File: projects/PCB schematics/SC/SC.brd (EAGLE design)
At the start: 160 x 100 mm, 19 parts

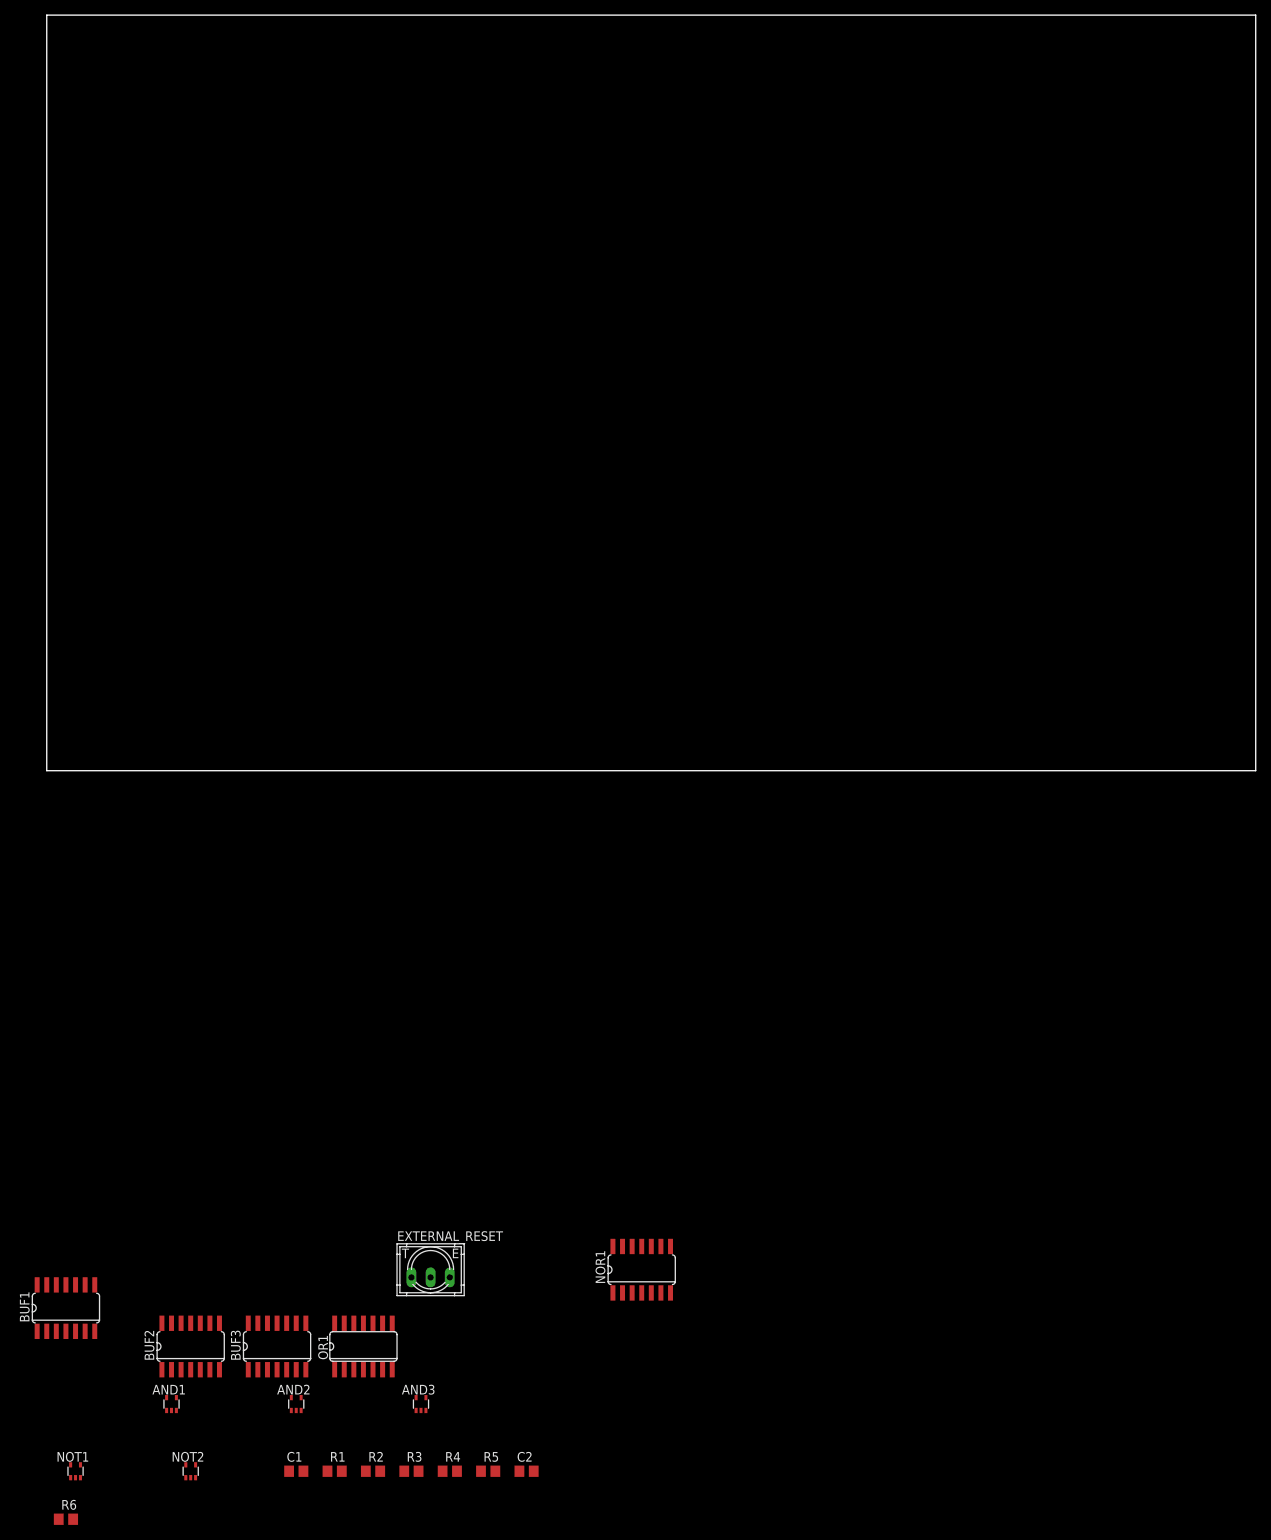
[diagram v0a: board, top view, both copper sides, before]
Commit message: SC - Rev A; First PCB revision complete.
This marks the first draft of the SC board.
Parts have been laid out and initial routing completed through
extensive use of autorouter.
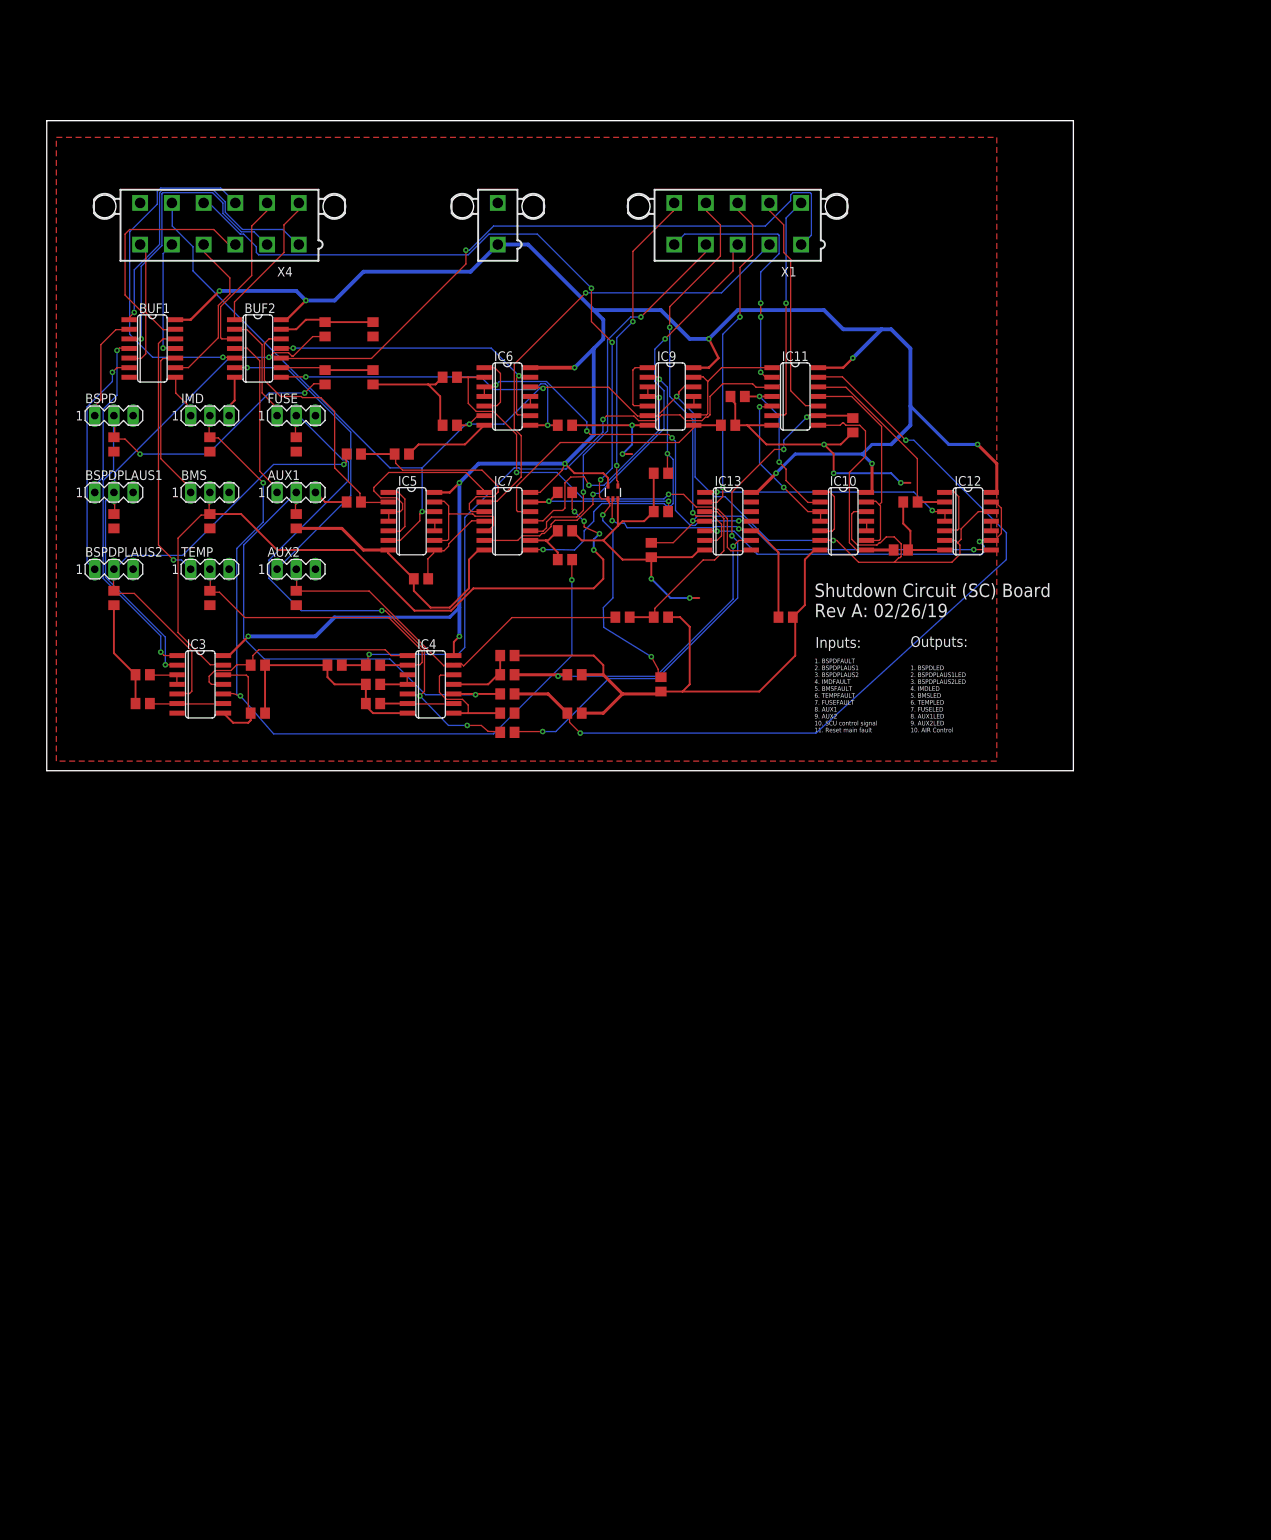
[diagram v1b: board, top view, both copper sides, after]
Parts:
- removed AND1, AND2, AND3: 74AHCT1G08DCK, 74xx-little-de:SC70-5
- removed BUF3: 7407D, 74xx-eu:SO14
- removed EXTERNAL_RESET: 9077-1, switch-misc:9077-1
- removed NOR1: 74LS33D, 74xx-eu:SO14
- removed NOT1, NOT2: 74LVC1G06DCK, 74xx-little-de:SC70-5
- removed OR1: 4072D, 40xx:SO14
- added AUX1, AUX2, BMS, BSPD, BSPDPLAUS1, BSPDPLAUS2, FUSE, IMD, TEMP: (no value), con-lstb:MA03-1
- added C10, C3, C4, C5, C6, C7, C8, C9: 1 uF, rcl:C0805
- added IC10, IC12, IC5, IC6, IC9: 74LS02D, 74xx-us:SO14
- added IC11, IC13, IC7: 74HC7014, IowaFormula:SO14
- added IC3, IC4: 74LS32D, 74xx-us:SO14
- added IC8: 74LVC1G08DCK, 74xx-little-us:SC70-5
- added R10, R11, R12, R13, R14, R15, R16, R17, R22, R23, R24, R25, R29, R30, R31, R35, R36, R37, R44, R45, R46, R7, R8, R9: 10k, rcl:R0805
- added R18, R19, R20, R21, R32, R33, R34, R41, R42, R43: 50k, rcl:R0805
- added X1: 5566-10, con-molex:5566-10
- added X2: 5566-2, con-molex:5566-2
- added X4: 5566-12, con-molex:5566-12
- BUF1, BUF2: value 7407D -> 74HC7014; device 74xx-eu:SO14 -> IowaFormula:SO14
- C2: value (none) -> 1 uF
- R1: value 50k -> 10k
- R2, R3, R4, R5, R6: value (none) -> 10k
- moved C2 146.2 mm to (43.2, 52.1), turned to 270 degrees
- moved R2 140.1 mm to (8.89, 43.2), turned to 90 degrees
- moved R4 139.5 mm to (21.6, 43.2), turned to 90 degrees
- moved BUF2 132.4 mm to (27.9, 55.9), turned to 270 degrees
- moved R5 131.0 mm to (21.6, 33.0), turned to 90 degrees
- moved R1 129.1 mm to (8.89, 33.0), turned to 90 degrees
- moved BUF1 127.5 mm to (14.0, 55.9), turned to 270 degrees
- moved R6 123.4 mm to (21.6, 22.9), turned to 90 degrees
- moved R3 122.1 mm to (8.89, 22.9), turned to 90 degrees
- moved C1 111.7 mm to (69.8, 12.7)
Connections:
- removed net +5V: EXTERNAL_RESET.1
- removed net AIR_CONTROL_SIGNAL: AND1.4, AND2.1, AND3.1, R3.2, R4.2
- removed net AIR_DELAY: AND3.2, BUF3.10, NOT2.2, R5.1
- removed net HV-_CONTROL: AND3.4
- removed net N$20: BUF3.11, C2.1, R4.1
- removed net N$21: AND2.2, NOT2.4
- removed net PRECHARGE_CONTROL: AND2.4
- removed net RESET: EXTERNAL_RESET.2, NOR1.6, R2.2
- removed net SET: BUF2.10, NOR1.2, R6.2
- removed net VDD: OR1.14
- removed net VSS: OR1.7
- new net AIR_CONTROL: IC8.4, X1.10
- new net AUX1: BUF2.3, X4.8
- new net AUX1_B: AUX1.1, BUF2.4
- new net AUX1_LED: IC13.2, X1.8
- new net AUX1_O: AUX1.2, IC4.10, R42.1, R8.2
- new net AUX2: BUF2.5, X4.9
- new net AUX2_B: AUX2.1, BUF2.6
- new net AUX2_LED: IC13.6, X1.9
- new net AUX2_O: AUX2.2, IC4.13, R43.1, R9.2
- new net BMSFAULT_LED: IC11.2, X1.5
- new net BMSFAULT_O: BMS.2, IC3.13, R33.1, R5.2
- new net BSPDFAULT_LED: BUF2.10, X1.1
- new net BSPDFAULT_O: BSPD.2, IC3.1, R19.1, R2.2
- new net BSPDPLAUS1_LED: IC7.2, X1.2
- new net BSPDPLAUS1_O: BSPDPLAUS1.2, IC3.2, R1.2, R20.1
- new net BSPDPLAUS2_LED: IC7.6, X1.3
- new net BSPDPLAUS2_O: BSPDPLAUS2.2, IC3.5, R21.1, R3.2
- new net FUSEFAULT_LED: IC11.10, X1.7
- new net FUSEFAULT_O: FUSE.2, IC4.5, R41.1, R7.2
- new net IMDFAULT_LED: IC7.10, X1.4
- new net IMDFAULT_O: IC3.10, IMD.2, R32.1, R4.2
- new net N$10: C7.1, IC11.3, R34.2
- new net N$11: IC4.11, R17.2, R18.1
- new net N$12: IC3.6, IC3.9, R11.2
- new net N$13: IC3.12, IC3.8, R12.2
- new net N$14: IC3.11, IC4.1, R13.2
- new net N$15: C8.1, IC11.9, R41.2
- new net N$16: C9.1, IC11.13, R42.2
- new net N$17: IC4.3, IC4.4, R14.2
- new net N$18: BUF2.9, C2.1, R19.2
- new net N$19: C10.1, IC13.3, R43.2
- new net N$2: IC4.12, IC4.8, R16.2
- new net N$3: IC3.3, IC3.4, R10.2
- new net N$4: BUF2.13, C3.1, R20.2
- new net N$7: C5.1, IC7.9, R32.2
- new net N$9: C6.1, IC7.13, R33.2
- new net Q_AUX1: IC12.3, IC12.4, IC13.1
- new net Q_AUX2: IC12.13, IC12.9, IC13.5
- new net Q_BMSFAULT: IC11.1, IC9.13, IC9.9
- new net Q_BSPDFAULT: BUF2.11, IC6.13, IC6.9
- new net Q_BSPDPLAUS1: IC5.3, IC5.4, IC7.1
- new net Q_BSPDPLAUS2: IC5.13, IC5.9, IC7.5
- new net Q_FUSEFAULT: IC10.13, IC10.9, IC11.11
- new net Q_IMDFAULT: IC7.11, IC9.3, IC9.4
- new net Q_TEMPFAULT: IC10.3, IC10.4, IC11.5
- new net RESET_MAINFAULT: IC10.12, IC10.6, IC12.12, IC12.6, IC5.12, IC5.6, IC6.12, IC6.6, IC9.12, IC9.6, R29.2, X4.11
- new net SET_AUX1: IC11.12, IC12.2, R45.2
- new net SET_AUX2: IC12.8, IC13.4, R46.2
- new net SET_BMSFAULT: IC7.12, IC9.8, R36.2
- new net SET_BSPDFAULT: BUF2.8, IC6.8, R22.2
- new net SET_BSPDPLAUS1: BUF2.12, IC5.2, R23.2
- new net SET_BSPDPLAUS2: IC5.8, IC7.4, R24.2
- new net SET_FUSEFAULT: IC10.8, IC11.8, R44.2
- new net SET_IMDFAULT: IC7.8, IC9.2, R35.2
- new net SET_MAINFAULT: IC13.8, IC6.2, R25.2
- new net SET_TEMPFAULT: IC10.2, IC11.4, R37.2
- new net TEMPFAULT_LED: IC11.6, X1.6
- new net TEMPFAULT_O: IC4.2, R34.1, R6.2, TEMP.2
- new net ~Q_AUX1: IC12.1, IC12.5
- new net ~Q_AUX2: IC12.10, IC12.11
- new net ~Q_BMSFAULT: IC9.10, IC9.11
- new net ~Q_BSPDFAULT: IC6.10, IC6.11
- new net ~Q_BSPDPLAUS1: IC5.1, IC5.5
- new net ~Q_BSPDPLAUS2: IC5.10, IC5.11
- new net ~Q_FUSEFAULT: IC10.10, IC10.11
- new net ~Q_IMDFAULT: IC9.1, IC9.5
- new net ~Q_TEMPFAULT: IC10.1, IC10.5
- net BMSFAULT: now also X4.5
- net BMSFAULT_B: now also BMS.1; no longer OR1.9
- net BSPDFAULT: now also X4.1
- net BSPDFAULT_B: now also BSPD.1; no longer OR1.2
- net BSPDPLAUS1: now also X4.2
- net BSPDPLAUS1_B: now also BSPDPLAUS1.1; no longer OR1.3
- net BSPDPLAUS2: now also X4.3
- net BSPDPLAUS2_B: now also BSPDPLAUS2.1; no longer OR1.4
- net FUSEFAULT: now also X4.7
- net FUSEFAULT_B: now also FUSE.1; no longer OR1.11
- net GND: now also AUX1.3, AUX2.3, BMS.3, BSPD.3, BSPDPLAUS1.3, BSPDPLAUS2.3, C10.2, C3.2, C4.2, C5.2, C6.2, C7.2, C8.2, C9.2, FUSE.3, IC10.7, IC11.7, IC12.7, IC13.7, IC3.7, IC4.7, IC5.7, IC6.7, IC7.7, IC8.3, IC9.7, IMD.3, R1.1, R10.1, R11.1, R12.1, R13.1, R14.1, R15.1, R16.1, R17.1, R22.1, R23.1, R24.1, R25.1, R29.1, R30.1, R31.1, R35.1, R36.1, R37.1, R4.1, R44.1, R45.1, R46.1, R5.1, R7.1, R8.1, R9.1, TEMP.3, X2.2; no longer AND1.3, AND2.3, AND3.3, BUF3.7, NOR1.7, NOT1.3, NOT2.3, R5.2
- net IMDFAULT: now also BUF1.9, X4.4; no longer BUF1.13
- net IMDFAULT_B: now also BUF1.8, IMD.1; no longer BUF1.12, OR1.10
- net N$1: now also IC4.6, IC4.9, R15.2; no longer OR1.1, OR1.12
- net N$5: now also C4.1, IC7.3, R21.2; no longer OR1.13, R1.1
- net N$6: now also IC13.9, R18.2; no longer BUF2.11, R1.2
- net N$8: now also IC13.10, IC8.2, R30.2; no longer AND1.2, NOT1.4
- net Q: now also IC13.11, IC6.3, IC6.4; no longer NOR1.3, NOR1.4, NOT1.2
- net SCU_CONTROL: now also IC8.1, R31.2, X4.10; no longer AND1.1
- net TEMPFAULT: now also BUF1.13, X4.6; no longer BUF1.9
- net TEMPFAULT_B: now also BUF1.12, TEMP.1; no longer BUF1.8, OR1.5
- net VCC: now also IC10.14, IC11.14, IC12.14, IC13.14, IC3.14, IC4.14, IC5.14, IC6.14, IC7.14, IC8.5, IC9.14, X2.1; no longer AND1.5, AND2.5, AND3.5, BUF3.14, NOR1.14, NOT1.5, NOT2.5
- net ~Q: now also IC6.1, IC6.5; no longer NOR1.1, NOR1.5
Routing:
- net VCC: track 0.00 -> 315.3 mm, vias 0 -> 12
- net GND: track 0.00 -> 306.7 mm, vias 0 -> 7
- net RESET_MAINFAULT: track 0.00 -> 195.2 mm, vias 0 -> 5
- net SCU_CONTROL: track 0.00 -> 119.0 mm, vias 0 -> 5
- net N$16: track 0.00 -> 113.7 mm, vias 0 -> 2
- net IMDFAULT_O: track 0.00 -> 108.0 mm, vias 0 -> 3
- net BMSFAULT_O: track 0.00 -> 102.2 mm, vias 0 -> 4
- net BSPDFAULT_LED: track 0.00 -> 88.2 mm, vias 0 -> 1
- net N$10: track 0.00 -> 86.9 mm, vias 0 -> 2
- net FUSEFAULT_O: track 0.00 -> 77.4 mm, vias 0 -> 3
- net BSPDFAULT_O: track 0.00 -> 73.1 mm, vias 0 -> 3
- net N$15: track 0.00 -> 72.4 mm, vias 0 -> 4
- net BSPDPLAUS1_O: track 0.00 -> 69.5 mm, vias 0 -> 2
- net AUX1_O: track 0.00 -> 66.4 mm, vias 0 -> 1
- net BSPDPLAUS1_LED: track 0.00 -> 62.0 mm, vias 0 -> 1
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- added copper zone on layer 1, net GND
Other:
- board size 160 x 100 mm -> 135.9 x 86 mm
- board text added: "1. BSPDFAULT 2. BSPDPLAUS1 3. BSPDPLAUS2 4. IMDFAULT 5. BMSFAULT 6. TEMPFAULT 7. FUSEFAULT 8. AUX1 9. AUX2 10. SCU control signal 11. Reset main fault"
- board text added: "1. BSPDLED 2. BSPDPLAUS1LED 3. BSPDPLAUS2LED 4. IMDLED 5. BMSLED 6. TEMPLED 7. FUSELED 8. AUX1LED 9. AUX2LED 10. AIR Control"
- board text added: "GND"
- board text added: "INPUT"
- board text added: "Inputs:"
- board text added: "Iowa Formula"
- board text added: "OUTPUT"
- board text added: "Outputs:"
- board text added: "Shutdown Circuit (SC) Board Rev A: 02/26/19"
- board text added: "VCC"

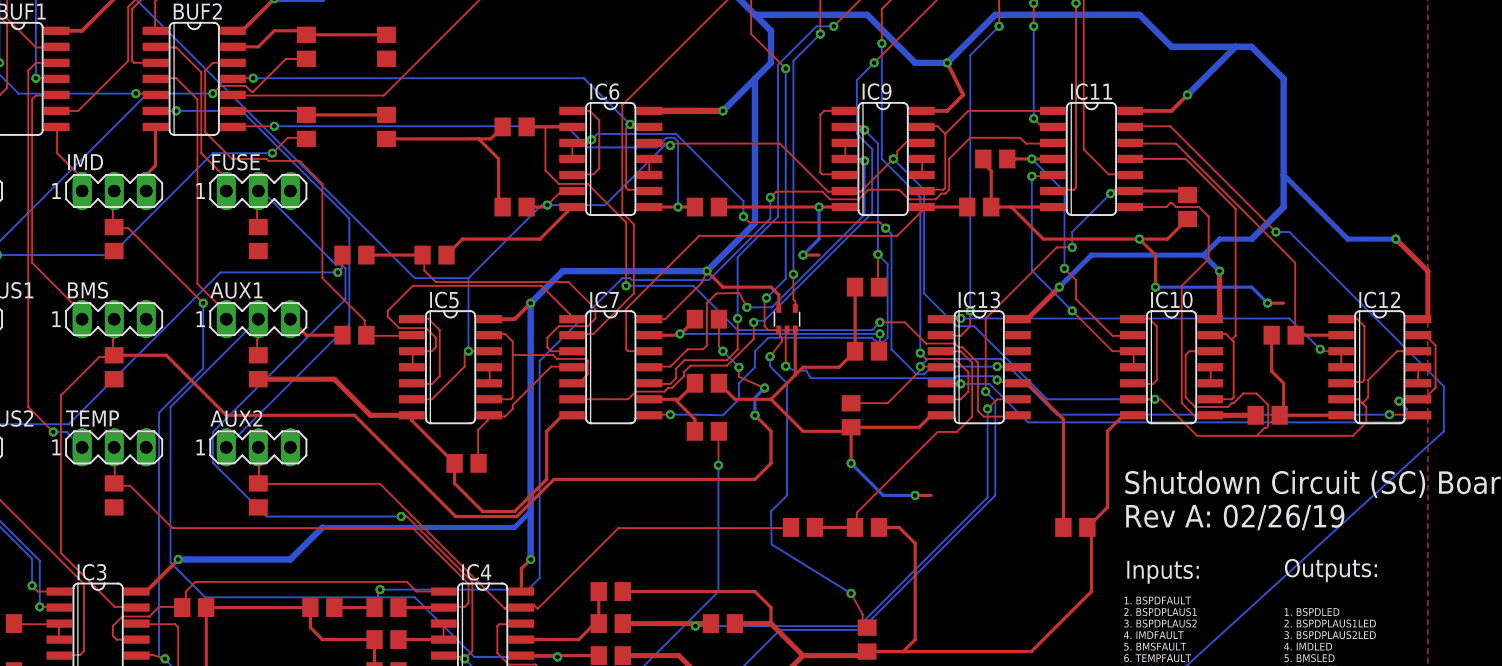
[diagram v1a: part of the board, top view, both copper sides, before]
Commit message: SC - Added component numbers/names.
Silkscreen was initially missing component names.
As many of the original components were resistors/capacitors,
Values were preferred.

However, standard board markup convention requires that part numbers
be given instead.

Note: Part numbers are given on EAGLE layer tNames, whereas values
are stated on tValues. Most CAM jobs will only import tNames onto
final Gerber file layer for board silkscreen.
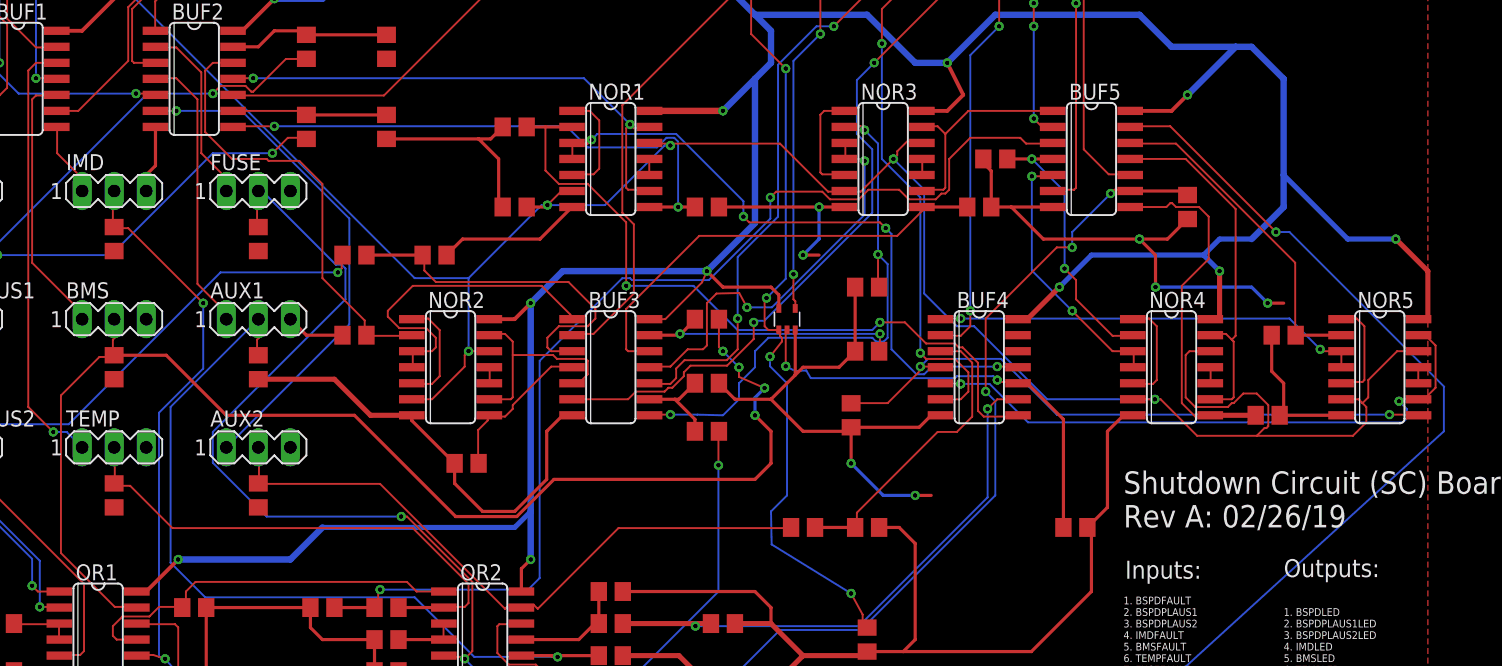
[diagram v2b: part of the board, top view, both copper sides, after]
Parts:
- renumbered IC10 to NOR4, IC11 to BUF5, IC12 to NOR5, IC13 to BUF4, IC3 to OR1, IC4 to OR2, IC5 to NOR2, IC6 to NOR1, IC7 to BUF3, IC8 to AND1, IC9 to NOR3
